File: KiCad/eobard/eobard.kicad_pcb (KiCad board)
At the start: 2 copper layers, 123.5 x 111.2 mm, 22 parts, among them J1 UART JACK LEFT, J3 UART Jack Right, SW1 SW_SPST, SW10 SW_SPST, SW11 SW_SPST, SW12 SW_SPST, SW13 SW_SPST, SW14 SW_SPST, SW15 SW_SPST, SW16 SW_SPST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

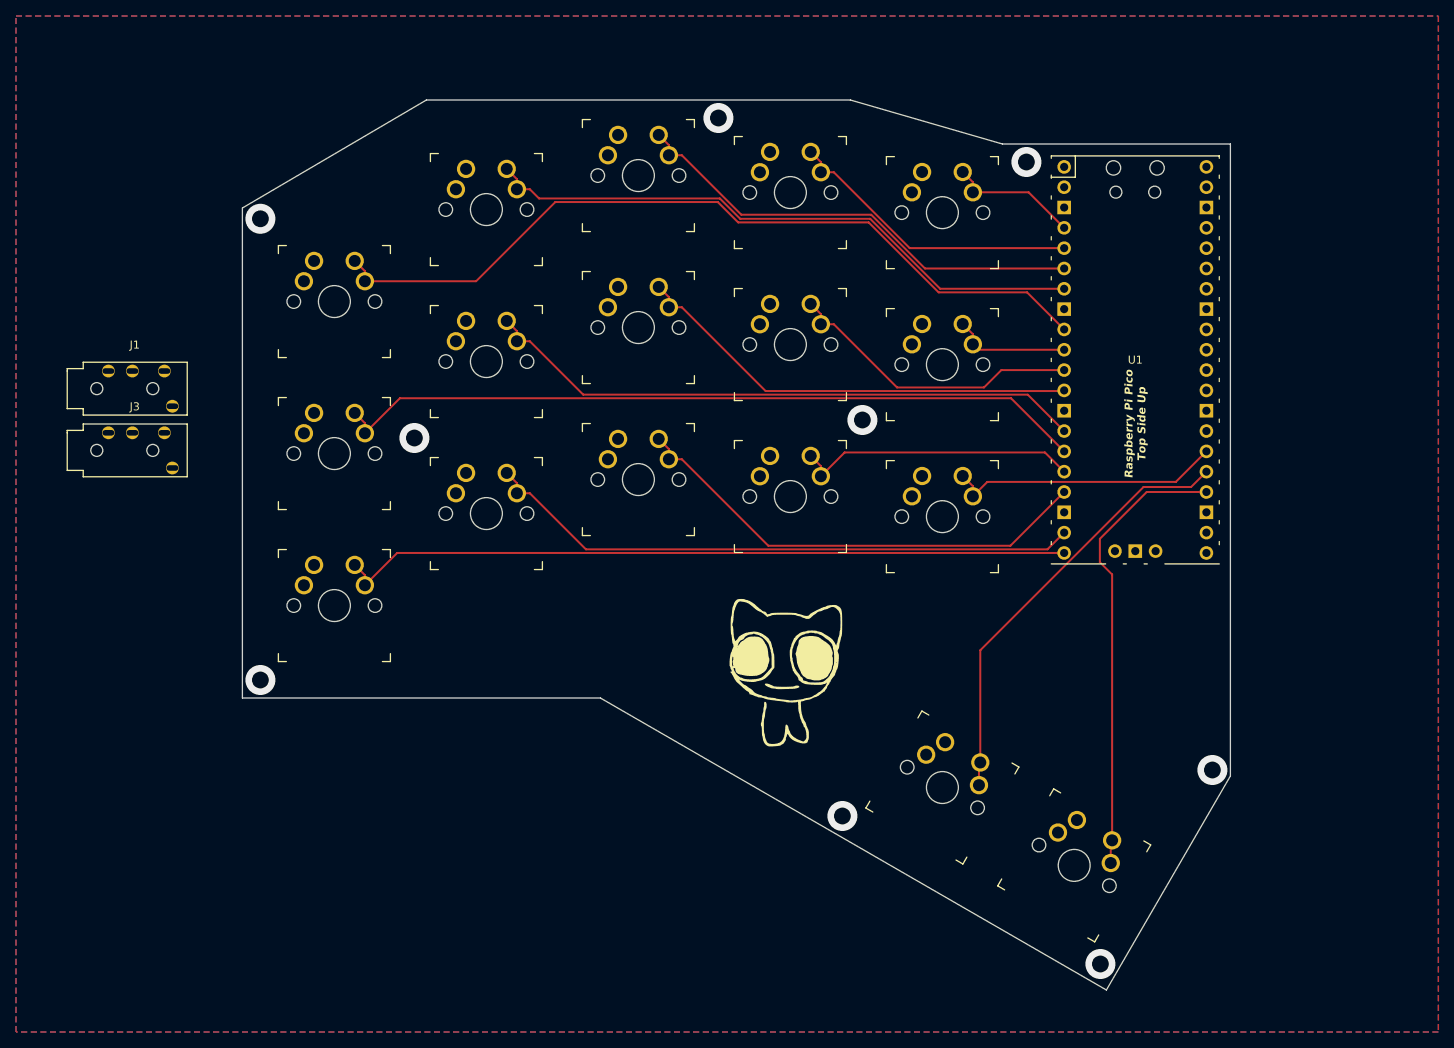
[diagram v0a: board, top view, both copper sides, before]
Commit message: Finished Initial Board Layout
Improving on the prototype. Gerbers are inside kicad folder.
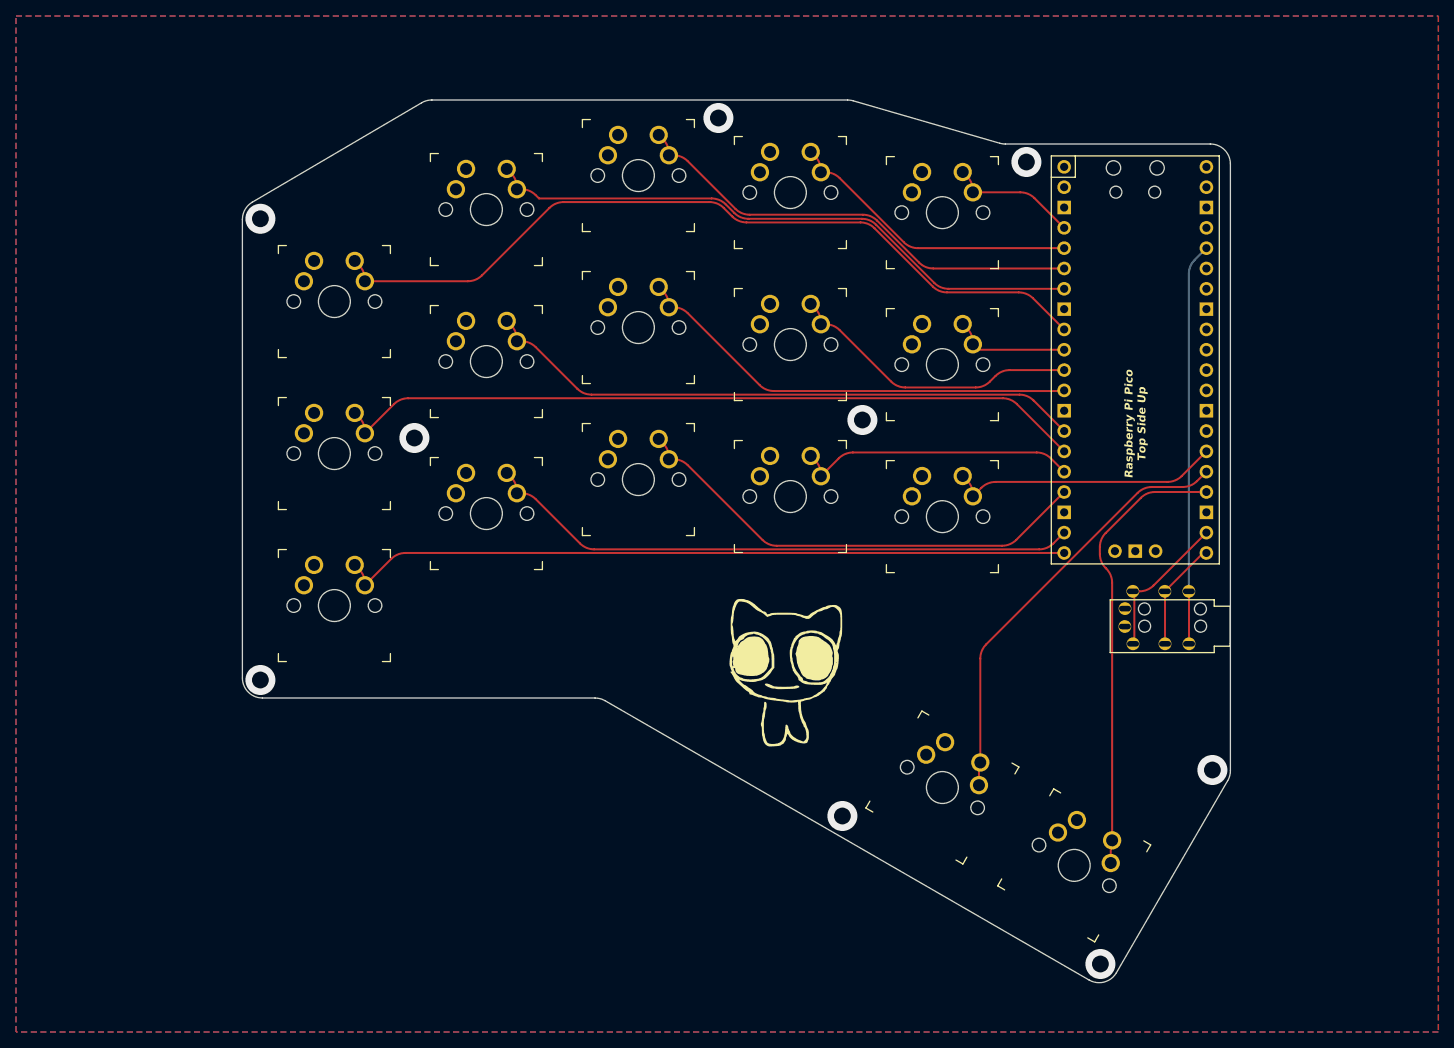
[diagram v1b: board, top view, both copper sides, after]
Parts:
- J3: moved to B.Cu
- moved J1 149.3 mm to (202.5, 107.0), turned to 180 degrees
- moved J3 146.7 mm to (202.5, 100.4), turned to 180 degrees
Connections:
- U1 pad 21: UART TX -> UART RX
- U1 pad 22: UART RX -> UART TX
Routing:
- net VCC: track 0.00 -> 50.3 mm
- net UART TX: track 0.00 -> 18.8 mm
- net UART RX: track 0.00 -> 13.7 mm
- net SW1: track 101.2 -> 100.2 mm
- net SW2: track 76.6 -> 75.9 mm
- net SW9: track 37.6 -> 37.0 mm
- net SW3: track 58.3 -> 57.7 mm
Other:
- board size 123.5 x 111.2 mm -> 123.5 x 110.3 mm
- board text removed: "RIGHT"
